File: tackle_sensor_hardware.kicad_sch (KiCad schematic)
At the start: 71 parts, among them J1 Conn_ARM_JTAG_SWD_10, J2 Conn_01x02_Male, J3 Conn_01x03_Male, J4 Conn_01x04_Male, Q1 DMP4051LK3, Q2 NCE0110K, SW1 PTS645SL43SMTR92 LFS, SW2 SW_DPDT_x2, T1 DRQ125-330-R, U1 STM32G031Fx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

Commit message: adding release v0.1
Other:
- note added: "+12V LED Output Current - Trip: 1.50 A Current - Hold: 750 mA Time to Trip: 100 ms"
- note removed: "+12V LED Output Current - Trip: 1.75 A Current - Hold: 350 mA Time to Trip: 100 ms"
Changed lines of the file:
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@@
     (effects (font (size 1.27 1.27)) (justify left bottom))
   )
-  (text "+12V LED Output\nCurrent - Trip: 1.75 A\nCurrent - Hold: 350 mA\nTime to Trip: 100 ms"
+  (text "+12V LED Output\nCurrent - Trip: 1.50 A\nCurrent - Hold: 750 mA\nTime to Trip: 100 ms"
     (at 307.34 118.11 0)
     (effects (font (size 1.27 1.27)) (justify left bottom))

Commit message: - updates for release v0.1
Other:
- title: (none) -> Tackle Sensor
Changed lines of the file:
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@@
 (kicad_sch (version 20211123) (generator eeschema)
   (paper "USLegal")
+  (title_block
+    (title "Tackle Sensor")
+    (date "2022-12-01")
+    (rev "v0.1")
+  )
   (junction (at 39.37 49.53) (diameter 0) (color 0 0 0 0)
   )

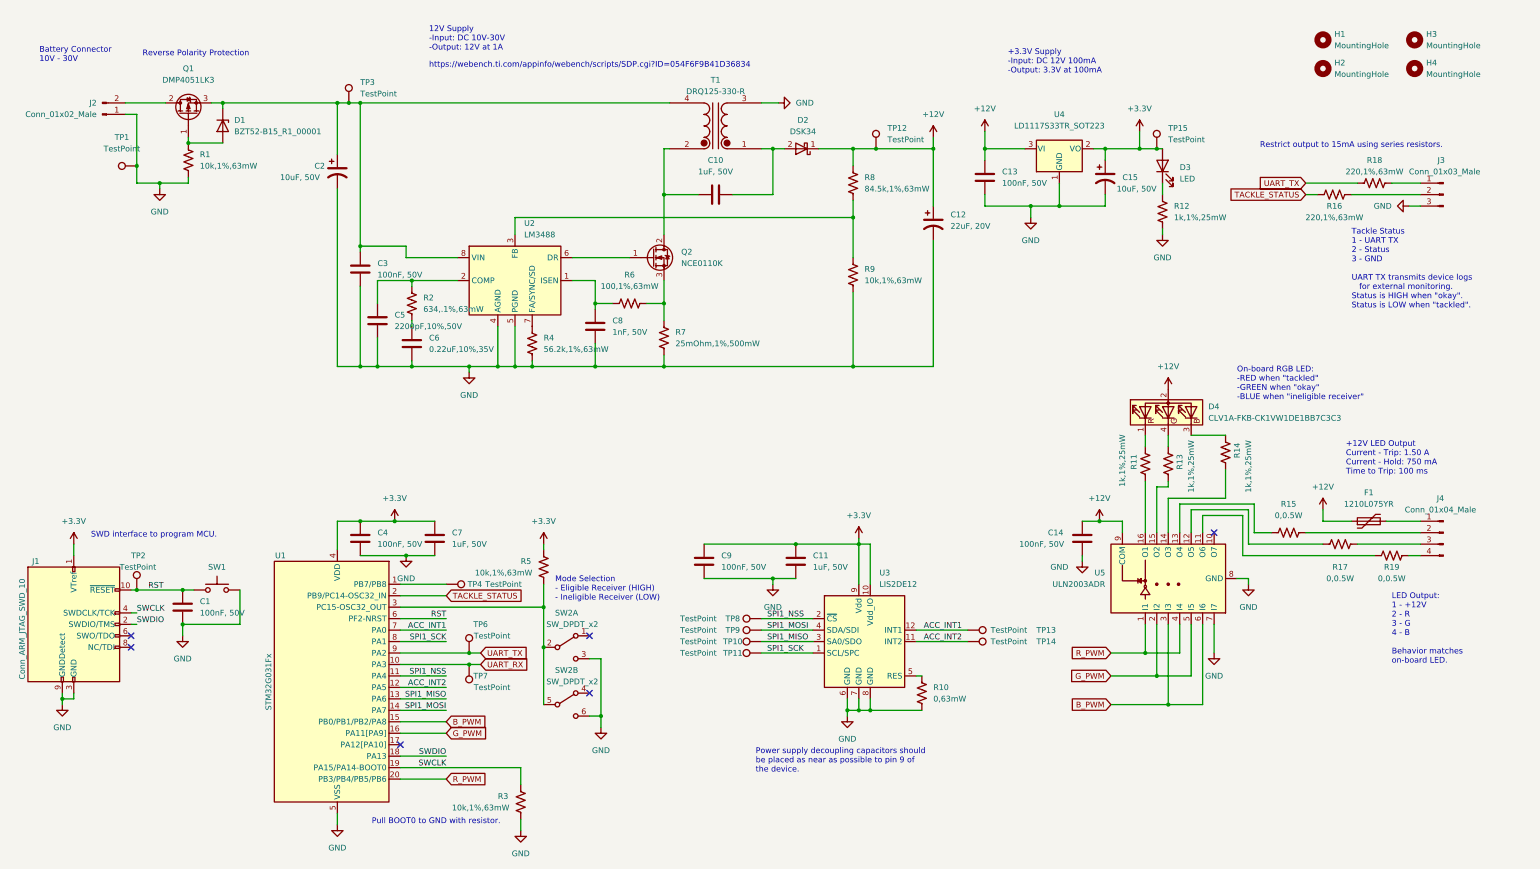
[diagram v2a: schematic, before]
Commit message: - added additional notes to the reference_sheet and the schematic sheet
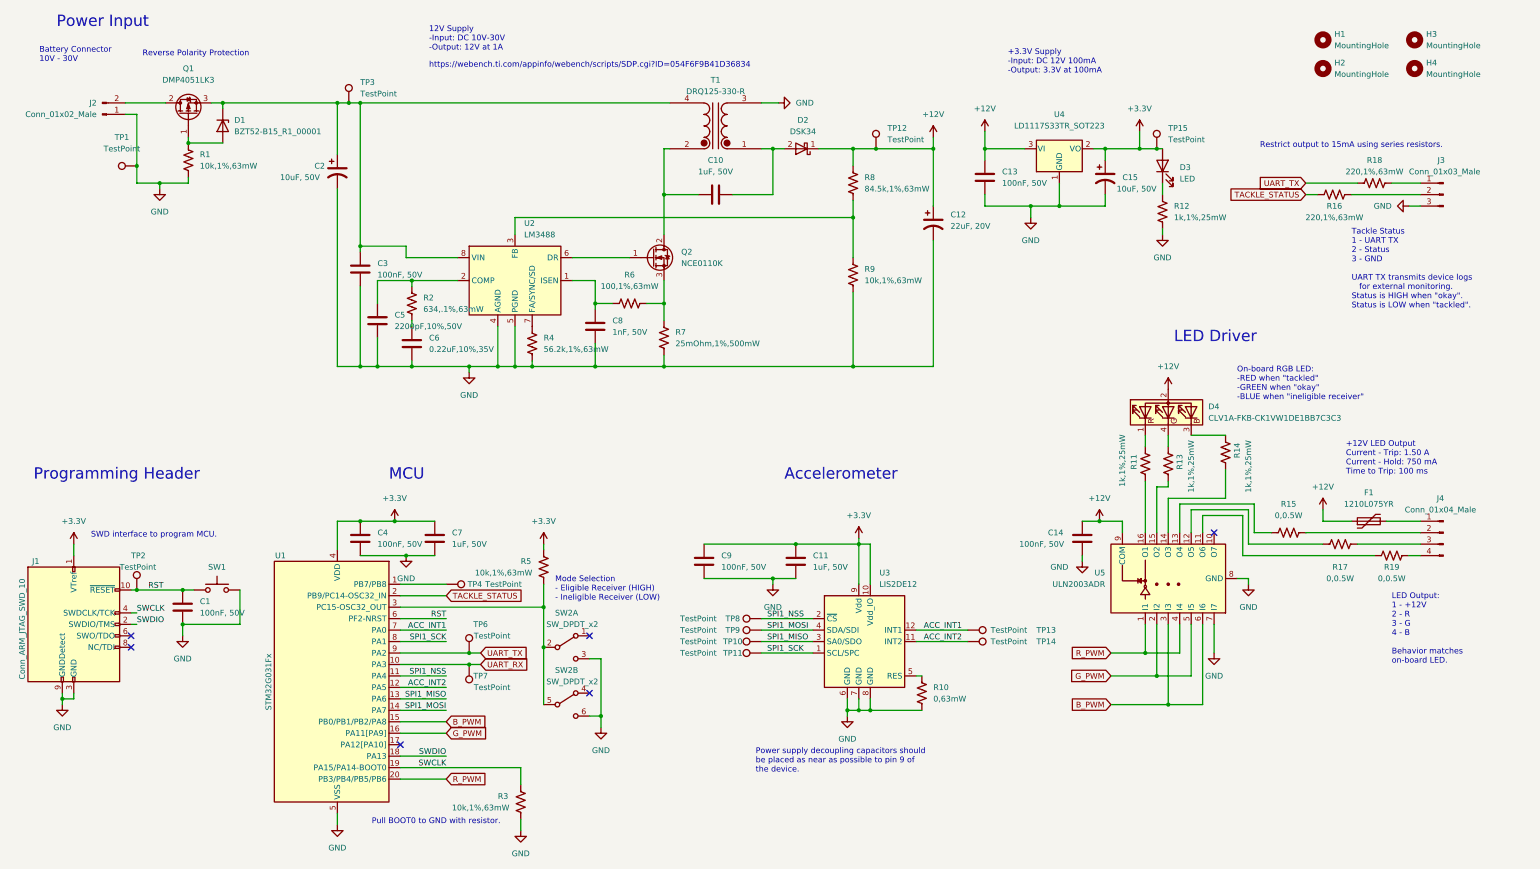
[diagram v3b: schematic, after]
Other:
- note added: "Accelerometer"
- note added: "LED Driver"
- note added: "MCU"
- note added: "Power Input"
- note added: "Programming Header"
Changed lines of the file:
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@@
     (stroke (width 0) (type default) (color 0 0 0 0))
+  )
+  (text "Programming Header" (at 16.51 119.38 0)
+    (effects (font (size 2.5 2.5)) (justify left bottom))
   )
   (text "Mode Selection\n- Eligible Receiver (HIGH)\n- Ineligible Receiver (LOW)"
     (at 132.08 146.05 0)
     (effects (font (size 1.27 1.27)) (justify left bottom))
+  )
+  (text "LED Driver" (at 269.24 88.9 0)
+    (effects (font (size 2.5 2.5)) (justify left bottom))
   )
   (text "12V Supply\n-Input: DC 10V-30V\n-Output: 12V at 1A" (at 104.14 24.13 0)
@@
     (at 232.41 29.21 0)
     (effects (font (size 1.27 1.27)) (justify left bottom))
+  )
+  (text "Power Input" (at 21.59 19.05 0)
+    (effects (font (size 2.5 2.5)) (justify left bottom))
   )
   (text "Tackle Status\n1 - UART TX\n2 - Status\n3 - GND\n\nUART TX transmits device logs \n   for external monitoring.\nStatus is HIGH when \"okay\".\nStatus is LOW when \"tackled\"."
@@
     (effects (font (size 1.27 1.27)) (justify left bottom))
   )
+  (text "MCU\n" (at 95.25 119.38 0)
+    (effects (font (size 2.5 2.5)) (justify left bottom))
+  )
   (text "Reverse Polarity Protection" (at 40.64 25.4 0)
     (effects (font (size 1.27 1.27)) (justify left bottom))
   )
+  (text "Accelerometer" (at 182.88 119.38 0)
+    (effects (font (size 2.5 2.5)) (justify left bottom))
+  )
   (text "https://webench.ti.com/appinfo/webench/scripts/SDP.cgi?ID=054F6F9B41D36834"

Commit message: - update PCB and schematic with new switch plus added 3d models
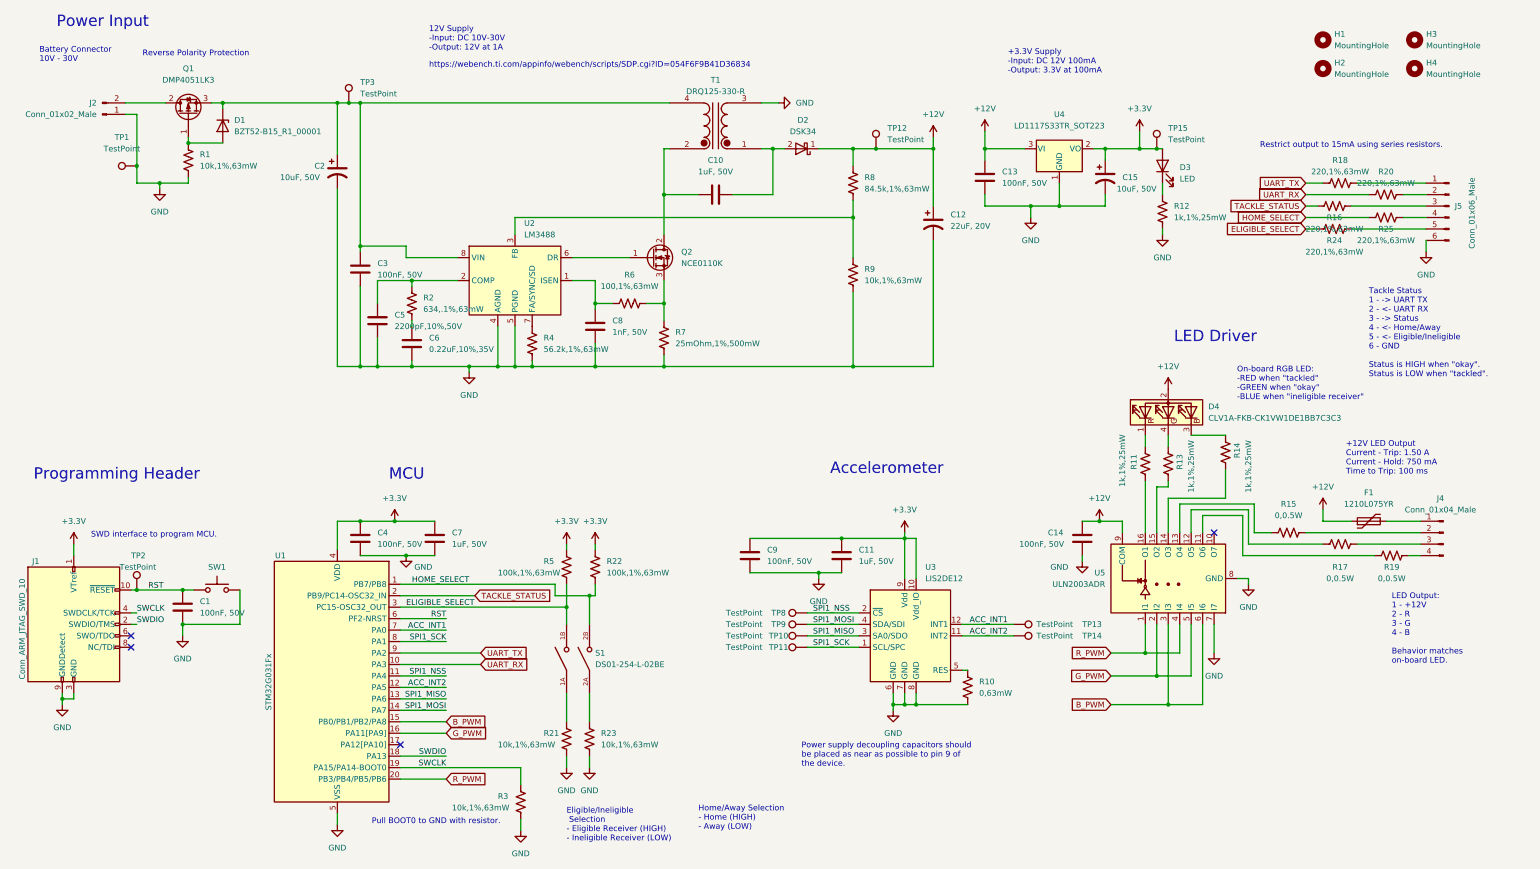
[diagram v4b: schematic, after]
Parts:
- removed J3: Conn_01x03_Male, Connector_JST:JST_XH_B3B-XH-A_1x03_P2.50mm_Vertical, symbol Connector:Conn_01x03_Male
- removed SW2: SW_DPDT_x2, rfc_footprint_lib:SS-3235S-L3, symbol Switch:SW_DPDT_x2
- removed TP4, TP7: TestPoint, TestPoint:TestPoint_Pad_D1.0mm, symbol Connector:TestPoint
- removed TP6: TestPoint, rfc_footprint_lib:test_point, symbol Connector:TestPoint
- added J5: Conn_01x06_Male, Connector_JST:JST_XH_B6B-XH-A_1x06_P2.50mm_Vertical, symbol Connector:Conn_01x06_Male
- added R20, R24, R25: 220,1%,63mW, Resistor_SMD:R_0402_1005Metric, symbol Device:R_US
- added R21, R23: 10k,1%,63mW, Resistor_SMD:R_0402_1005Metric, symbol Device:R_US
- added R22: 100k,1%,63mW, Resistor_SMD:R_0402_1005Metric, symbol Device:R_US
- added S1: DS01-254-L-02BE, rfc_footprint_lib:SW_DS01-254-L-02BE, symbol DS01-254-L-02BE:DS01-254-L-02BE
- R5: value 10k,1%,63mW -> 100k,1%,63mW; JLCPN C25744 -> (none); MPN 0402WGF1002TCE -> (none)
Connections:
- net +3V3: now also R22.1
- net GND: now also J5.6 (Pin_6), R21.2, R23.2
- net UART_RX: now also R20.1
- net at R18.2: now also J5.1 (Pin_1)
- net at R16.2: now also J5.3 (Pin_3)
- net ELIGIBLE_SELECT: now reaches R5.2, U1.3 (PC15-OSC32_OUT)
- net ELIGIBLE_SELECT: now also R24.1, S1.1B
- net HOME_SELECT: now reaches U1.1 (PB7/PB8)
- net HOME_SELECT: now also R22.2, R25.1, S1.2B
- new net: J5.2 (Pin_2), R20.2
- new net: J5.4 (Pin_4), R25.2
- new net: J5.5 (Pin_5), R24.2
- new net: R23.1, S1.2A
- new net: R21.1, S1.1A
- no-connect marks 6 -> 4
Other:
- note added: "Eligible/Ineligible Selection - Eligible Receiver (HIGH) - Ineligible Receiver (LOW)"
- note added: "Home/Away Selection - Home (HIGH) - Away (LOW)"
- note added: "Tackle Status 1 - -> UART TX 2 - <- UART RX 3 - -> Status 4 - <- Home/Away 5 - <- Eligible/Ineligible 6 - GND Status is HIGH when "okay". Status is LOW when "tackled"."
- note removed: "Mode Selection - Eligible Receiver (HIGH) - Ineligible Receiver (LOW)"
- note removed: "Tackle Status 1 - UART TX 2 - Status 3 - GND UART TX transmits device logs for external monitoring. Status is HIGH when "okay". Status is LOW when "tackled"."
- moved on the sheet: C11, C9, R10, R16, R18, R5, TP10, TP11, TP13, TP14, TP8, TP9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

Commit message: - finish routing
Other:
- note removed: "On-board RGB LED: -RED when "tackled" -GREEN when "okay" -BLUE when "ineligible receiver""
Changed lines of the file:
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@@
-    (effects (font (size 1.27 1.27)) (justify left bottom))
-  )
-  (text "On-board RGB LED:\n-RED when \"tackled\"\n-GREEN when \"okay\"\n-BLUE when \"ineligible receiver\""
-    (at 283.21 101.6 0)
     (effects (font (size 1.27 1.27)) (justify left bottom))
   )

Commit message: - updating layout and releasing
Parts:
- added FID1, FID2, FID3: Fiducial, Fiducial:Fiducial_0.5mm_Mask1.5mm, symbol Mechanical:Fiducial
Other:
- moved on the sheet: R16, R20, R25

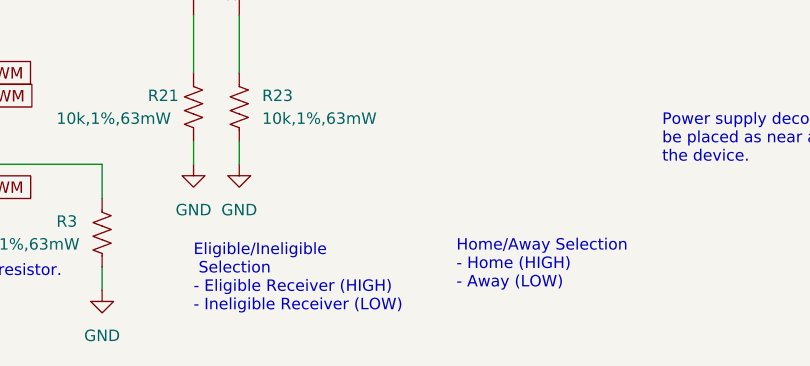
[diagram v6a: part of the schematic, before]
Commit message: - regen. schematic with Logic level updates
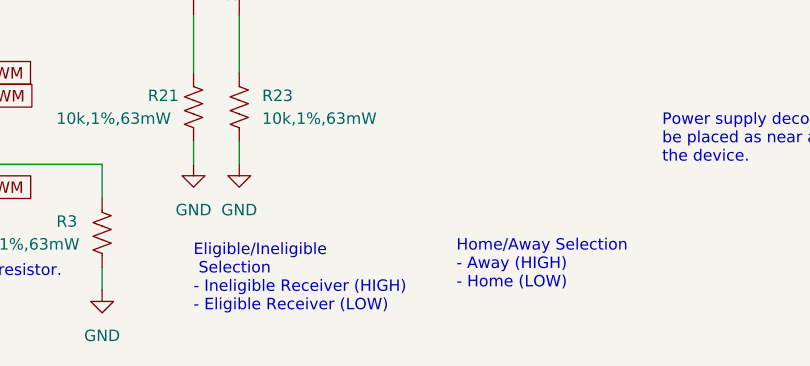
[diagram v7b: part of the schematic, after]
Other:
- note added: "Eligible/Ineligible Selection - Ineligible Receiver (HIGH) - Eligible Receiver (LOW)"
- note added: "Home/Away Selection - Away (HIGH) - Home (LOW)"
- note removed: "Eligible/Ineligible Selection - Eligible Receiver (HIGH) - Ineligible Receiver (LOW)"
- note removed: "Home/Away Selection - Home (HIGH) - Away (LOW)"
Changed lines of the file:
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@@
     (effects (font (size 2.5 2.5)) (justify left bottom))
   )
-  (text "Eligible/Ineligible\n Selection\n- Eligible Receiver (HIGH)\n- Ineligible Receiver (LOW)"
+  (text "Eligible/Ineligible\n Selection\n- Ineligible Receiver (HIGH)\n- Eligible Receiver (LOW)"
     (at 134.62 199.39 0)
     (effects (font (size 1.27 1.27)) (justify left bottom))
@@
     (effects (font (size 1.27 1.27)) (justify left bottom))
   )
-  (text "Home/Away Selection\n- Home (HIGH)\n- Away (LOW)" (at 163.83 196.85 0)
+  (text "Home/Away Selection\n- Away (HIGH)\n- Home (LOW)" (at 163.83 196.85 0)
     (effects (font (size 1.27 1.27)) (justify left bottom))
   )
